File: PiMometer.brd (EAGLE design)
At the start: 62.5 x 41.9 mm, 32 parts, among them IC1 MAX6675, IC2 MAX6675, IC3 MAX6675, IC4 MAX6675

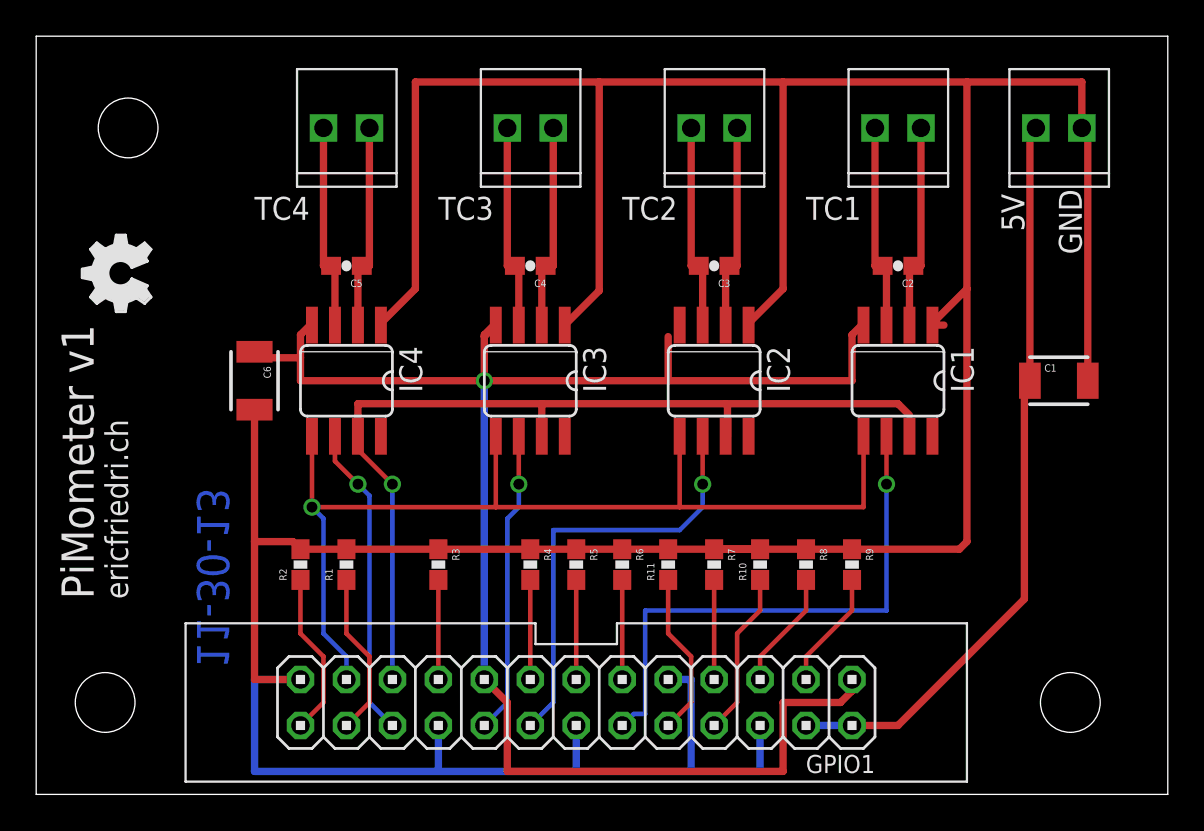
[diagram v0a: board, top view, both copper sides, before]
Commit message: Added package.json and rpi.js
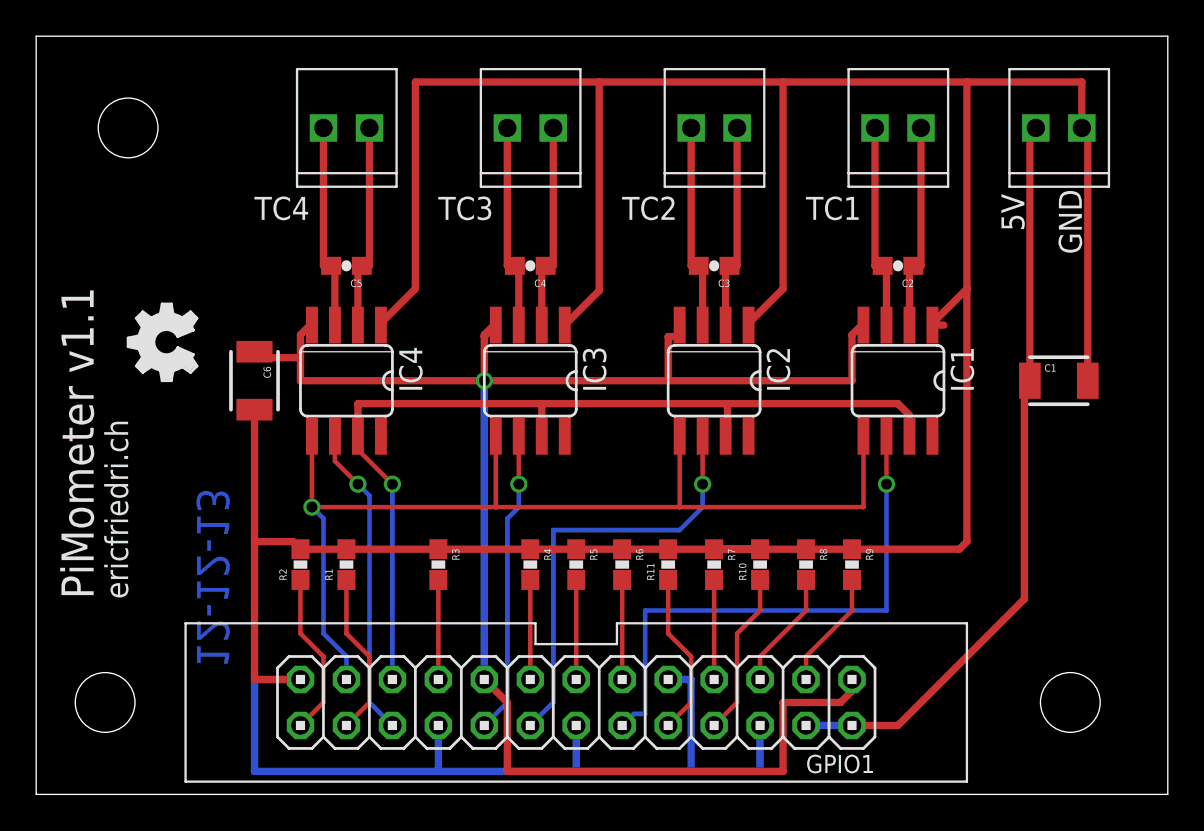
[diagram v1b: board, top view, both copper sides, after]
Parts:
- moved U$1 4.58 mm to (8.89, 22.9)
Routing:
- net 3V3: track 92.5 -> 93.7 mm
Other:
- board text added: "12-12-13"
- board text added: "PiMometer v1.1"
- board text removed: "11-30-13"
- board text removed: "PiMometer v1"
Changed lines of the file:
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@@
 <wire x1="62.535" y1="41.9" x2="0" y2="41.9" width="0" layer="20"/>
 <wire x1="0" y1="41.9" x2="0" y2="0" width="0" layer="20"/>
-<text x="8.89" y="6.985" size="1.778" layer="16" font="vector" ratio="18" rot="SMR90">11-30-13</text>
-<text x="3.175" y="10.795" size="1.778" layer="25" rot="R90">PiMometer v1</text>
+<text x="8.89" y="6.985" size="1.778" layer="16" font="vector" ratio="18" rot="SMR90">12-12-13</text>
+<text x="3.175" y="10.795" size="1.778" layer="25" rot="R90">PiMometer v1.1</text>
 <text x="5.08" y="10.795" size="1.27" layer="25" rot="R90">ericfriedri.ch</text>
 <text x="12.065" y="31.75" size="1.27" layer="25">TC4</text>
@@
 <attribute name="PROD_ID" value="CAP-09824" x="12.065" y="22.86" size="1.778" layer="27" rot="R270" display="off"/>
 </element>
-<element name="U$1" library="ohw-logo" package="OSHW_FILLX150_NOTEXT" value="" x="6.35" y="26.67" rot="R90"/>
+<element name="U$1" library="ohw-logo" package="OSHW_FILLX150_NOTEXT" value="" x="8.89" y="22.86" rot="R90"/>
 <element name="STANDOFF1" library="SparkFun-Electromechanical" package="STAND-OFF" value="STAND-OFF" x="5.08" y="36.83"/>
 <element name="STANDOFF2" library="SparkFun-Electromechanical" package="STAND-OFF" value="STAND-OFF" x="57.15" y="5.08"/>
@@
 <contactref element="IC2" pad="4"/>
 <wire x1="45.6184" y1="25.9334" x2="45.72" y2="25.9334" width="0" layer="19" extent="1-1"/>
-<wire x1="35.56" y1="25.9334" x2="34.925" y2="25.2984" width="0" layer="19" extent="1-1"/>
+<wire x1="34.925" y1="25.2984" x2="35.56" y2="25.2984" width="0.4064" layer="1"/>
+<wire x1="35.56" y1="25.2984" x2="35.56" y2="25.9334" width="0.4064" layer="1"/>
 </signal>
 <signal name="GND">
